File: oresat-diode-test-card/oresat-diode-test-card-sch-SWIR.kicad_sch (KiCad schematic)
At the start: 31 parts, among them Q4 DMP3050LVT-7, Q5 PMV45EN, U13 TLV6001DCK, U4 TLV6001DCK, U8 NX3L4051-Q100, U9 TLV6001DCK

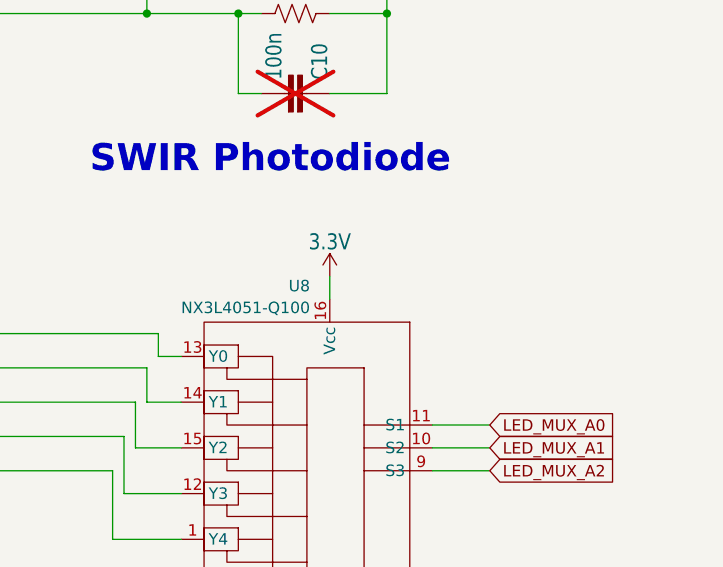
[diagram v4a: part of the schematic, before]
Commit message: Fix OPD weirdness, lots of little polishing including power plane movement and thicker traces.
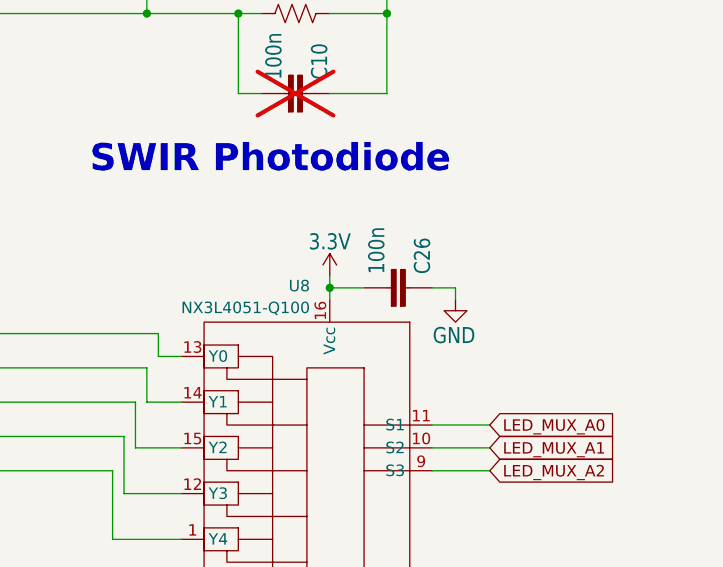
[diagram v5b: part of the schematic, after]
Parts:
- added C26: 100n, oresat-passives:0603-C-NOSILK, symbol oresat-proto-card-eagle-import:C-EU0603-C-NOSILK
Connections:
- net 3.3V: now also C26.2
- net GND: now also C26.1
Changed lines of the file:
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@@
 	)
 	(junction
+		(at 276.86 111.76)
+		(diameter 0)
+		(color 0 0 0 0)
+	)
+	(junction
 		(at 212.09 144.78)
 		(diameter 0)
@@
 	(wire
 		(pts
-			(xy 276.86 110.49) (xy 276.86 113.03)
+			(xy 276.86 110.49) (xy 276.86 111.76)
 		)
 		(stroke
@@
 	(wire
 		(pts
+			(xy 288.29 111.76) (xy 290.83 111.76)
+		)
+		(stroke
+			(width 0)
+			(type default)
+		)
+	)
+	(wire
+		(pts
+			(xy 276.86 111.76) (xy 276.86 113.03)
+		)
+		(stroke
+			(width 0)
+			(type default)
+		)
+	)
+	(wire
+		(pts
 			(xy 251.46 204.47) (xy 251.46 213.36)
 		)
@@
 	(wire
 		(pts
+			(xy 290.83 111.76) (xy 290.83 113.03)
+		)
+		(stroke
+			(width 0)
+			(type default)
+		)
+	)
+	(wire
+		(pts
 			(xy 196.85 110.49) (xy 196.85 114.3)
 		)
@@
 	(wire
 		(pts
+			(xy 276.86 111.76) (xy 280.67 111.76)
+		)
+		(stroke
+			(width 0)
+			(type default)
+		)
+	)
+	(wire
+		(pts
 			(xy 212.09 139.7) (xy 203.2 139.7)
 		)
@@
 	(symbol
 		(lib_id "power:GND")
+		(at 290.83 113.03 0)
+		(unit 1)
+		(exclude_from_sim no)
+		(in_bom yes)
+		(on_board yes)
+		(dnp no)
+		(property "Reference" "#GND030"
+			(at 290.83 113.03 0)
+			(effects
+				(font
+					(size 1.27 1.27)
+				)
+				(hide yes)
+			)
+		)
+		(property "Value" "GND"
+			(at 288.29 118.11 0)
+			(effects
+				(font
+					(size 1.778 1.5113)
+				)
+				(justify left bottom)
+			)
+		)
+		(property "Footprint" ""
+			(at 290.83 113.03 0)
+			(effects
+				(font
+					(size 1.27 1.27)
+				)
+				(hide yes)
+			)
+		)
+		(property "Datasheet" ""
+			(at 290.83 113.03 0)
+			(effects
+				(font
+					(size 1.27 1.27)
+				)
+				(hide yes)
+			)
+		)
+		(property "Description" "Power symbol creates a global label with name \"GND\" , ground"
+			(at 290.83 113.03 0)
+			(effects
+				(font
+					(size 1.27 1.27)
+				)
+				(hide yes)
+			)
+		)
+		(pin "1"
+		)
+		(instances
+			(project "oresat-diode-test-card"
+				(path "/04d32576-d084-475b-9eac-d7f3fd9579d7/a25fadb6-76d8-445f-be27-cd15465f11e4"
+					(reference "#GND030")
+					(unit 1)
+				)
+			)
+		)
+	)
+	(symbol
+		(lib_id "power:GND")
 		(at 152.4 143.51 0)
 		(unit 1)
@@
 					(unit 1)
 				)
+			)
+		)
+	)
+	(symbol
+		(lib_id "oresat-proto-card-eagle-import:C-EU0603-C-NOSILK")
+		(at 285.75 111.76 270)
+		(mirror x)
+		(unit 1)
+		(exclude_from_sim no)
+		(in_bom yes)
+		(on_board yes)
+		(dnp no)
+		(property "Reference" "C26"
+			(at 286.131 110.236 0)
+			(effects
+				(font
+					(size 1.778 1.5113)
+				)
+				(justify left bottom)
+			)
+		)
+		(property "Value" "100n"
+			(at 281.051 110.236 0)
+			(effects
+				(font
+					(size 1.778 1.5113)
+				)
+				(justify left bottom)
+			)
+		)
+		(property "Footprint" "oresat-passives:0603-C-NOSILK"
+			(at 285.75 111.76 0)
+			(effects
+				(font
+					(size 1.27 1.27)
+				)
+				(hide yes)
+			)
+		)
+		(property "Datasheet" ""
+			(at 285.75 111.76 0)
+			(effects
+				(font
+					(size 1.27 1.27)
+				)
+				(hide yes)
+			)
+		)
+		(property "Description" ""
+			(at 285.75 111.76 0)
+			(effects
+				(font
+					(size 1.27 1.27)
+				)
+				(hide yes)
+			)
+		)
+		(property "DIS" "Digi-Key"
+			(at 285.75 111.76 0)
+			(effects
+				(font
+					(size 1.27 1.27)
+				)
+				(justify left bottom)
+				(hide yes)
+			)
+		)
+		(property "DPN" "1276-1001-1-ND"
+			(at 285.75 111.76 0)
+			(effects
+				(font
+					(size 1.27 1.27)
+				)
+				(justify left bottom)
+				(hide yes)
+			)
+		)
+		(property "MFR" "Samsung"
+			(at 285.75 111.76 0)
+			(effects
+				(font
+					(size 1.27 1.27)
+				)
+				(justify left bottom)
+				(hide yes)
+			)
+		)
+		(property "MPN" "CL05B104KO5NNNC"
+			(at 285.75 111.76 0)
+			(effects
+				(font
+					(size 1.27 1.27)
+				)
+				(justify left bottom)
+				(hide yes)
+			)
+		)
+		(pin "2"
+		)
+		(pin "1"
+		)
+		(instances
+			(project "oresat-diode-test-card"
+				(path "/04d32576-d084-475b-9eac-d7f3fd9579d7/a25fadb6-76d8-445f-be27-cd15465f11e4"
+					(reference "C26")
+					(unit 1)
+				)

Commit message: Added BOM
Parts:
- C10, C12, C24, C25, C26, C6, C7: DST (none) -> Digi-Key
- Q5: DIS (none) -> Digi-Key

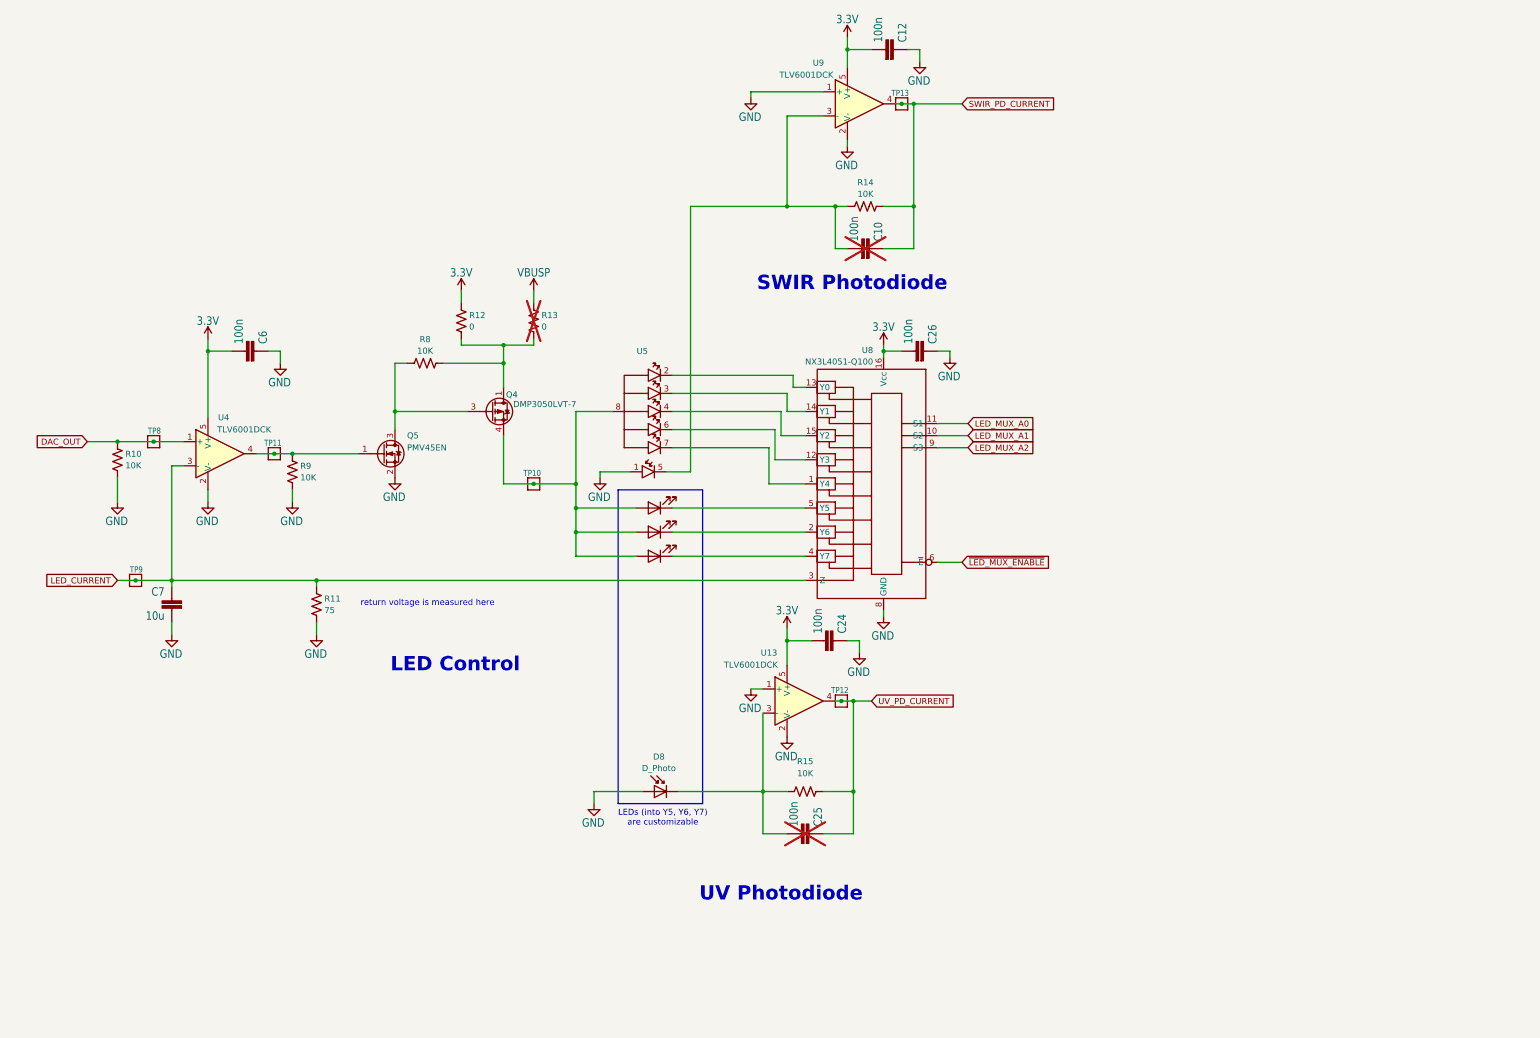
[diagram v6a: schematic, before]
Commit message: BOM changes! Now up to date.
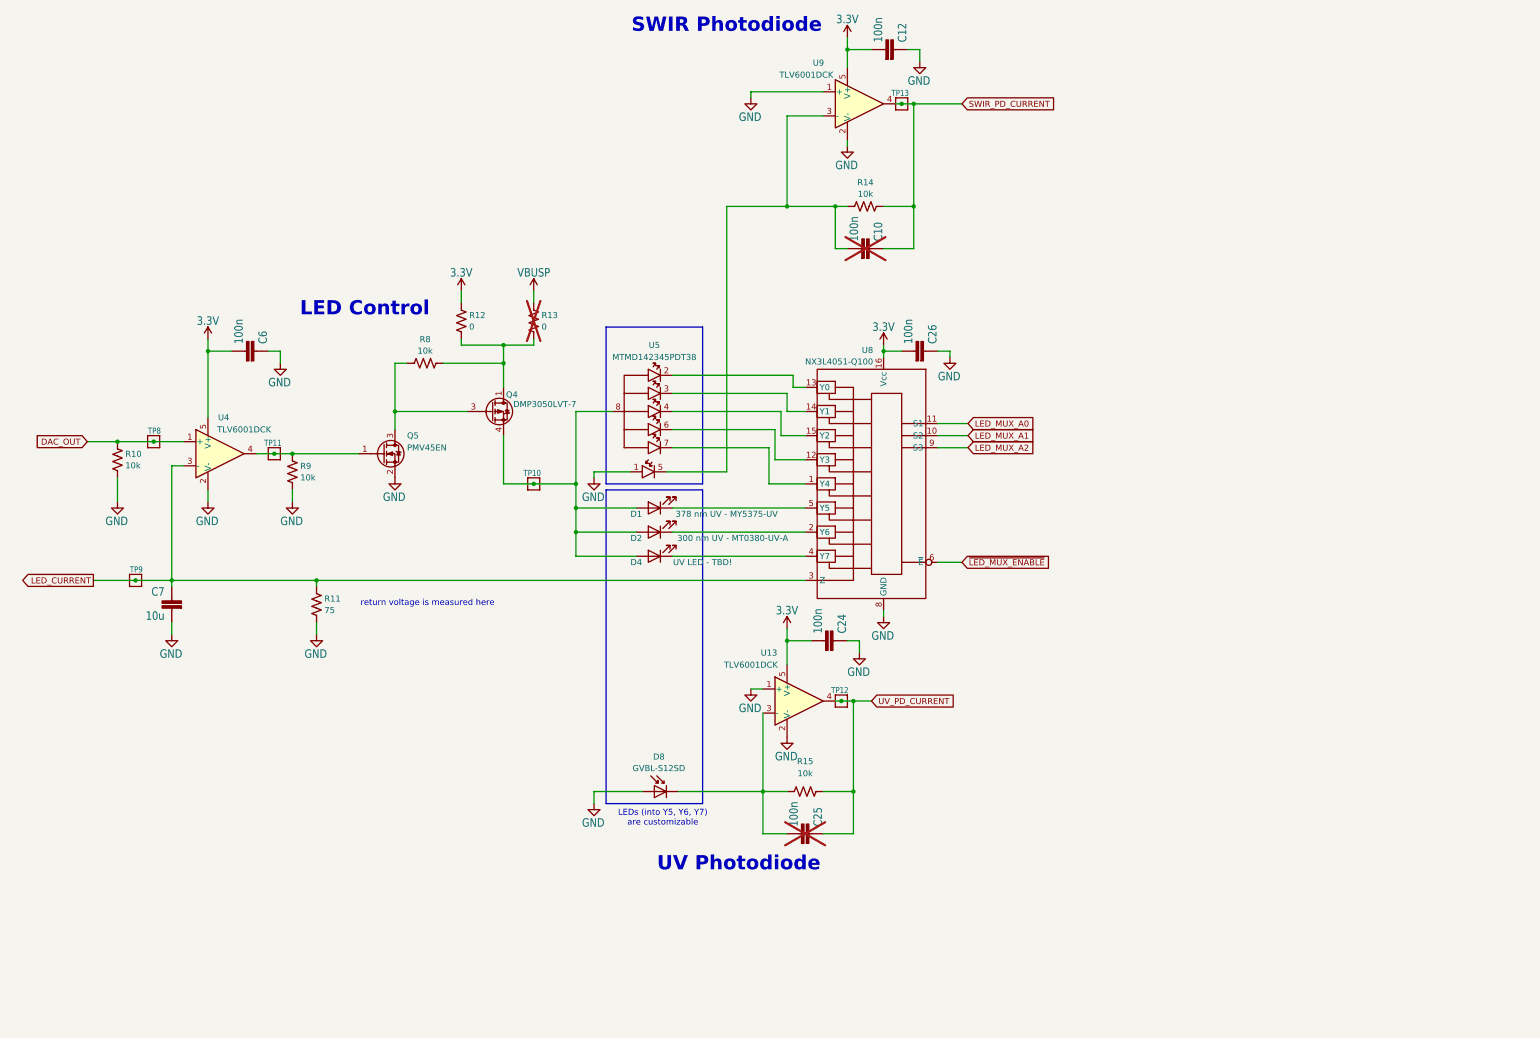
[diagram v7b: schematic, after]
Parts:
- C10, C25, Q5: DIS Digi-Key -> (none); DST Digi-Key -> DigiKey
- C12, C24, C26, C6: DIS Digi-Key -> (none); DPN 1276-1001-1-ND -> 587-3472-1-ND; DST Digi-Key -> DigiKey; MFR Samsung -> Taiyo Yuden; MPN CL05B104KO5NNNC -> TMK107BJ104KAHT
- C7: DIS Digi-Key -> (none); DPN 1276-1001-1-ND -> 490-12317-1-ND; DST Digi-Key -> DigiKey; MFR Samsung -> Murata Electronics; MPN CL05B104KO5NNNC -> GRT188R61C106KE13D
- D1: value LED -> 378 nm UV - MY5375-UV; DPN (none) -> 1125-1406-ND; DST (none) -> DigiKey; MFR (none) -> Marktech Optoelectronics; MPN (none) -> MT5375-UV
- D2: value LED -> 300 nm UV - MT0380-UV-A; DPN (none) -> 1125-1180-ND; DST (none) -> DigiKey; MFR (none) -> Marktech Optoelectronics; MPN (none) -> MT0380-UV-A
- D4: value LED -> UV LED - TBD!; DPN (none) -> N/A; DST (none) -> N/A; MFR (none) -> N/A; MPN (none) -> N/A
- D8: value D_Photo -> GVBL-S12SD; DPN (none) -> 2096-GVBL-S12SDCT-ND; DST (none) -> DigiKey; MFR (none) -> Genicom Co., Ltd.; MPN (none) -> GVBL-S12SD
- Q4: DPN (none) -> DMP3050LVT-7DICT-ND; DST (none) -> DigiKey; MFR (none) -> Diodes Inc; MPN (none) -> DMP3050LVT-7
- R10, R14, R15, R8, R9: value 10K -> 10k; DPN (none) -> RMCF0603FT10K0CT-ND; DST (none) -> DigiKey; MFR (none) -> Stackpole Electronics Inc; MPN (none) -> RMCF0603FT10K0
- R11: DPN (none) -> RMCF0603FT75R0CT-ND; DST (none) -> DigiKey; MFR (none) -> Stackpole Electronics Inc; MPN (none) -> RMCF0603FT75R0
- R12: DPN (none) -> RMCF0603ZT0R00CT-ND; DST (none) -> DigiKey; MFR (none) -> Stackpole Electronics Inc; MPN (none) -> RMCF0603ZT0R00
- R13: DST (none) -> DigiKey
- TP10, TP11, TP12, TP13, TP8, TP9: DPN (none) -> N/A; DST (none) -> N/A; MFR (none) -> N/A; MPN (none) -> N/A; now left out of the parts list
- U13, U4, U9: DPN (none) -> 296-45125-1-ND; DST (none) -> DigiKey; MFR (none) -> Texas Instruments; MPN (none) -> TLV6001UIDBVR
- U5: value ~ -> MTMD142345PDT38; DPN (none) -> N/A; DST (none) -> N/A; MFR (none) -> marktech Optoelectronics; MPN (none) -> MTMD142345PDT38
- U8: DPN (none) -> 568-12394-1-ND; DST (none) -> DigiKey; MFR (none) -> NXP USA Inc.; MPN (none) -> NX3L4051PW-Q100J

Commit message: Fixed package for op amps :(
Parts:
- U13, U4, U9: DPN 296-45125-1-ND -> 296-51689-1-ND; MPN TLV6001UIDBVR -> TLV6001QDCKRQ1
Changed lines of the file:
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@@
 			)
 		)
-		(property "Datasheet" "https://www.ti.com/general/docs/suppproductinfo.tsp?distId=10&gotoUrl=https%3A%2F%2Fwww.ti.com%2Flit%2Fgpn%2Ftlv6001"
+		(property "Datasheet" "https://www.ti.com/general/docs/suppproductinfo.tsp?distId=10&gotoUrl=https%3A%2F%2Fwww.ti.com%2Flit%2Fgpn%2Ftlv6001-q1"
 			(at 134.62 133.35 0)
 			(effects
@@
 			)
 		)
-		(property "Description" "General Purpose Amplifier 1 Circuit Rail-to-Rail SOT-23-5"
+		(property "Description" "General Purpose Amplifier 1 Circuit Rail-to-Rail SC-70-5"
 			(at 134.62 133.35 0)
 			(effects
@@
 			)
 		)
-		(property "DPN" "296-45125-1-ND"
+		(property "DPN" "296-51689-1-ND"
 			(at 134.62 133.35 0)
 			(effects
@@
 			)
 		)
-		(property "MPN" "TLV6001UIDBVR"
+		(property "MPN" "TLV6001QDCKRQ1"
 			(at 134.62 133.35 0)
 			(effects
@@
 			)
 		)
-		(property "Datasheet" "https://www.ti.com/general/docs/suppproductinfo.tsp?distId=10&gotoUrl=https%3A%2F%2Fwww.ti.com%2Flit%2Fgpn%2Ftlv6001"
+		(property "Datasheet" "https://www.ti.com/general/docs/suppproductinfo.tsp?distId=10&gotoUrl=https%3A%2F%2Fwww.ti.com%2Flit%2Fgpn%2Ftlv6001-q1"
 			(at 256.54 185.42 0)
 			(effects
@@
 			)
 		)
-		(property "Description" "General Purpose Amplifier 1 Circuit Rail-to-Rail SOT-23-5"
+		(property "Description" "General Purpose Amplifier 1 Circuit Rail-to-Rail SC-70-5"
 			(at 256.54 185.42 0)
 			(effects
@@
 			)
 		)
-		(property "DPN" "296-45125-1-ND"
+		(property "DPN" "296-51689-1-ND"
 			(at 256.54 185.42 0)
 			(effects
@@
 			)
 		)
-		(property "MPN" "TLV6001UIDBVR"
+		(property "MPN" "TLV6001QDCKRQ1"
 			(at 256.54 185.42 0)
 			(effects
@@
 			)
 		)
-		(property "Datasheet" "https://www.ti.com/general/docs/suppproductinfo.tsp?distId=10&gotoUrl=https%3A%2F%2Fwww.ti.com%2Flit%2Fgpn%2Ftlv6001"
+		(property "Datasheet" "https://www.ti.com/general/docs/suppproductinfo.tsp?distId=10&gotoUrl=https%3A%2F%2Fwww.ti.com%2Flit%2Fgpn%2Ftlv6001-q1"
 			(at 269.24 59.69 0)
 			(effects
@@
 			)
 		)
-		(property "Description" "General Purpose Amplifier 1 Circuit Rail-to-Rail SOT-23-5"
+		(property "Description" "General Purpose Amplifier 1 Circuit Rail-to-Rail SC-70-5"
 			(at 269.24 59.69 0)
 			(effects
@@
 			)
 		)
-		(property "DPN" "296-45125-1-ND"
+		(property "DPN" "296-51689-1-ND"
 			(at 269.24 59.69 0)
 			(effects
@@
 			)
 		)
-		(property "MPN" "TLV6001UIDBVR"
+		(property "MPN" "TLV6001QDCKRQ1"
 			(at 269.24 59.69 0)
 			(effects
